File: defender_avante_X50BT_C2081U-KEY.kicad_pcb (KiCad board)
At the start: 2 copper layers, 172.7 x 61 mm, 85 parts, among them CN301 CONNECTOR_M_006_20_SPECIAL, J300 JUMPER, J301 JUMPER, J302 JUMPER, J303 JUMPER, J304 JUMPER, J305 JUMPER, J306 JUMPER, J307 JUMPER, J308 JUMPER, J309 JUMPER, J310 JUMPER, J311 JUMPER, J312 JUMPER, J313 JUMPER, J314 JUMPER, J315 JUMPER, J316 JUMPER, J317 JUMPER, J318 JUMPER, J319 JUMPER, J320 JUMPER, J321 JUMPER, J322 JUMPER, J323 JUMPER, J324 JUMPER, J325 JUMPER, J326 JUMPER, J327 JUMPER, J328 JUMPER, J329 JUMPER, J330 JUMPER, J331 JUMPER, J332 JUMPER, J333 JUMPER, J334 JUMPER, J335 JUMPER, J336 JUMPER, J337 JUMPER, Q300 BJT_NPN_GENERAL, U300 TM1668

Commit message: Исправлены связи новых резисторов. Удалены примитивы на слоях F.Cu и F.Mask
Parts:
- turned R306 to 90 degrees
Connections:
- D300 pad A: /E -> /KS1
- D301 pad A: /D -> /KS2
- D302 pad A: /DP -> /KS3
- D303 pad A: /C -> /KS4
- D304 pad A: /G -> /KS5
- R306 pad 1: V -> /IC_+5V
- R306 pad 2: /IC_+5V -> V
- R318 pad 1: Net-(R318-Pad1) -> /E
- R318 pad 2: /E -> /KS1
- R319 pad 1: Net-(R319-Pad1) -> /D
- R319 pad 2: /D -> /KS2
- R320 pad 1: Net-(R320-Pad1) -> /DP
- R320 pad 2: /DP -> /KS3
- R321 pad 1: Net-(R321-Pad1) -> /C
- R321 pad 2: /C -> /KS4
- R322 pad 1: Net-(R322-Pad1) -> /G
- R322 pad 2: /G -> /KS5
- R323 pad 1: Net-(R323-Pad1) -> /F
- R323 pad 2: /F -> Net-(R323-Pad2)
- R324 pad 2: /B -> /A
- R325 pad 2: /A -> /B
- U300 pad 1: Net-(U300-Pad1) -> /IC_DATA
- U300 pad 10: Net-(U300-Pad10) -> /KS4
- U300 pad 11: Net-(U300-Pad11) -> /KS5
- U300 pad 12: Net-(U300-Pad12) -> Net-(R323-Pad2)
- U300 pad 13: Net-(U300-Pad13) -> Net-(R325-Pad1)
- U300 pad 14: Net-(U300-Pad14) -> Net-(R324-Pad1)
- U300 pad 2: Net-(U300-Pad2) -> /IC_CLK
- U300 pad 20: Net-(U300-Pad20) -> /DIG4
- U300 pad 21: Net-(U300-Pad21) -> /DIG3
- U300 pad 22: Net-(U300-Pad22) -> COM
- U300 pad 23: Net-(U300-Pad23) -> /DIG2
- U300 pad 24: Net-(U300-Pad24) -> /DIG1
- U300 pad 3: Net-(U300-Pad3) -> /STB
- U300 pad 5: Net-(U300-Pad5) -> /K2
- U300 pad 6: Net-(U300-Pad6) -> /IC_+5V
- U300 pad 7: Net-(U300-Pad7) -> /KS1
- U300 pad 8: Net-(U300-Pad8) -> /KS2
- U300 pad 9: Net-(U300-Pad9) -> /KS3

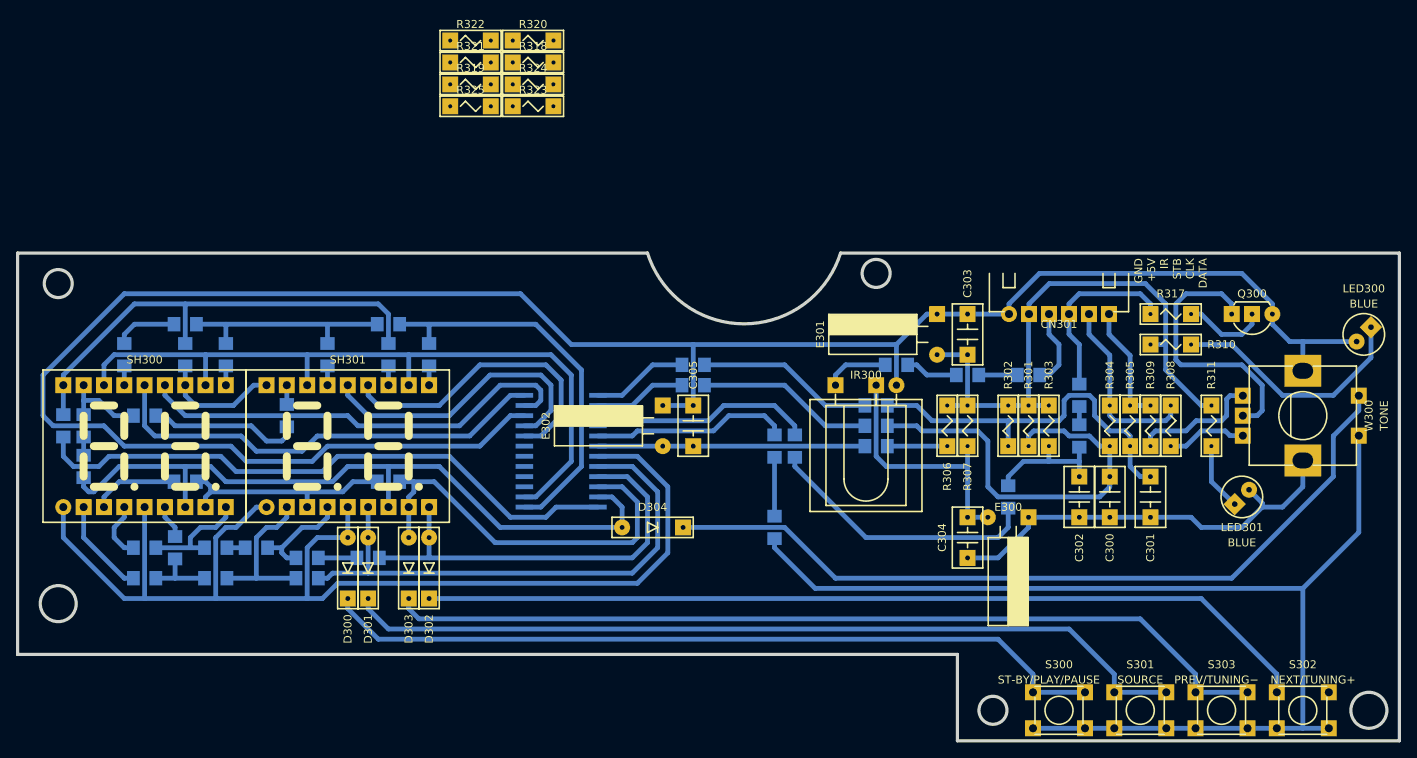
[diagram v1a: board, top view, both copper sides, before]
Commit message: Токоограничивающие резисторы размещены на плате. Плата отредактирована
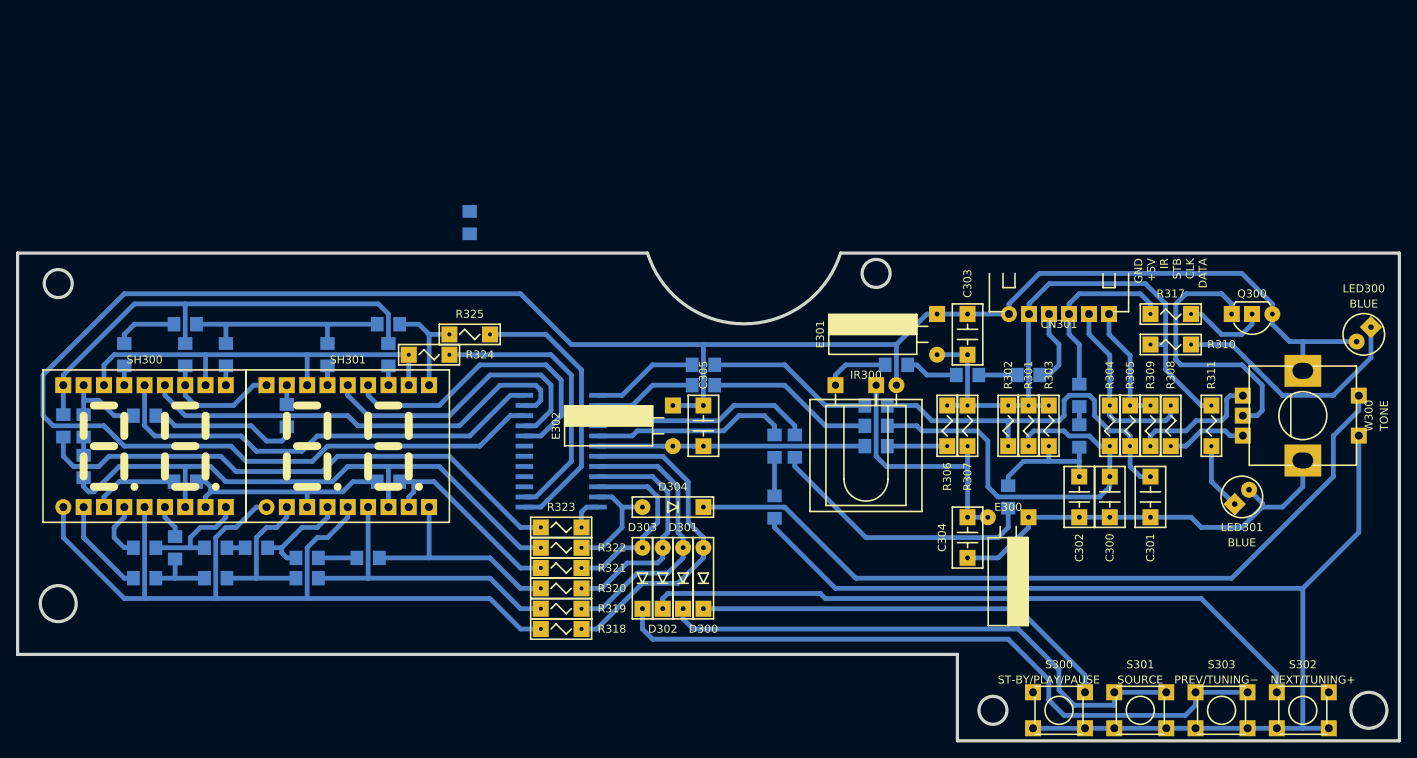
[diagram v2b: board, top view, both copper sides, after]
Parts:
- moved R318 70.9 mm to (129.5, 121.9)
- moved R320 68.6 mm to (129.5, 116.8)
- moved R319 66.5 mm to (129.5, 119.4)
- moved R322 64.4 mm to (129.5, 111.8)
- moved R321 64.2 mm to (129.5, 114.3)
- moved R323 52.8 mm to (129.5, 109.2)
- moved D300 44.5 mm to (147.3, 115.6)
- moved D301 39.4 mm to (144.8, 115.6)
- moved R324 36.2 mm to (113.0, 87.6), turned to 180 degrees
- moved D302 29.2 mm to (142.2, 115.6)
- moved D303 29.2 mm to (139.7, 115.6)
- moved R325 28.5 mm to (118.1, 85.1), turned to 180 degrees
- moved J314 17.3 mm to (118.1, 71.1)
- moved D304 3.59 mm to (143.5, 106.7)
- moved J311 2.54 mm to (156.2, 106.7)
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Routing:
- net Net-(D300-PadC): track 99.1 -> 53.3 mm
- net /KS1: track 0.00 -> 41.8 mm
- net /A: track 92.5 -> 52.6 mm
- net /B: track 93.8 -> 55.6 mm
- net Net-(D301-PadC): track 106.7 -> 69.2 mm
- net /E: track 146.2 -> 109.5 mm
- net /KS2: track 0.00 -> 35.5 mm
- net Net-(R324-Pad1): track 0.00 -> 34.8 mm
- net Net-(R325-Pad1): track 0.00 -> 34.6 mm
- net /KS3: track 0.00 -> 29.8 mm
- net /D: track 112.7 -> 83.0 mm
- net Net-(D302-PadC): track 112.2 -> 84.7 mm
- net /DP: track 95.1 -> 69.6 mm
- net Net-(D303-PadC): track 111.8 -> 86.3 mm
- net /C: track 89.5 -> 64.5 mm
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
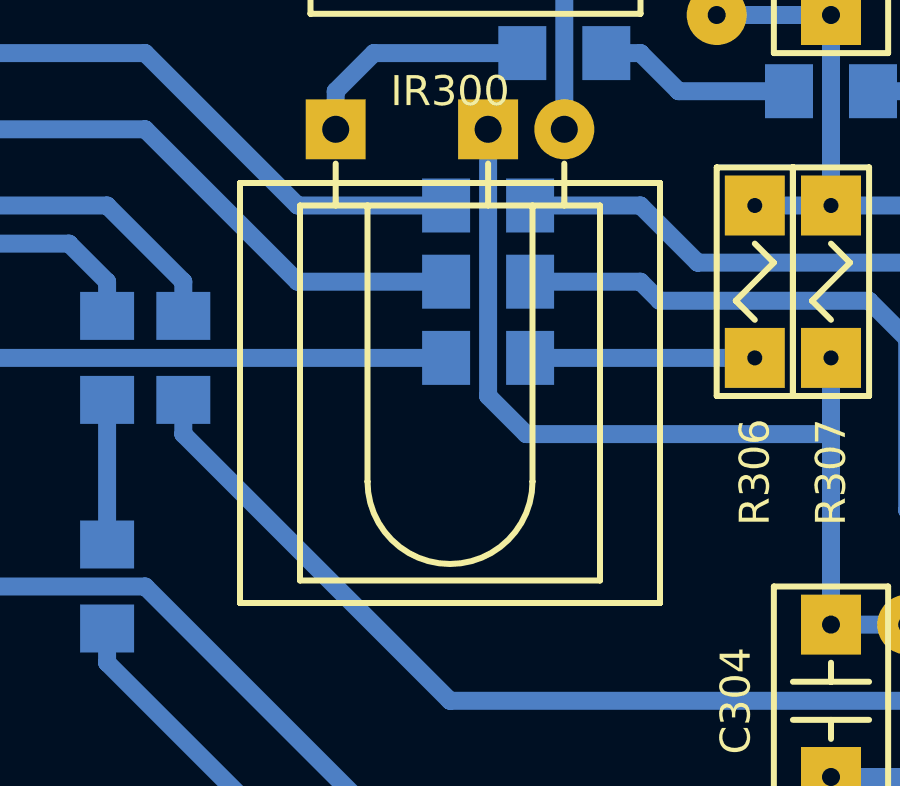
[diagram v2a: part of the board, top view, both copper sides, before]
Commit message: Удалён поролоновый держатель
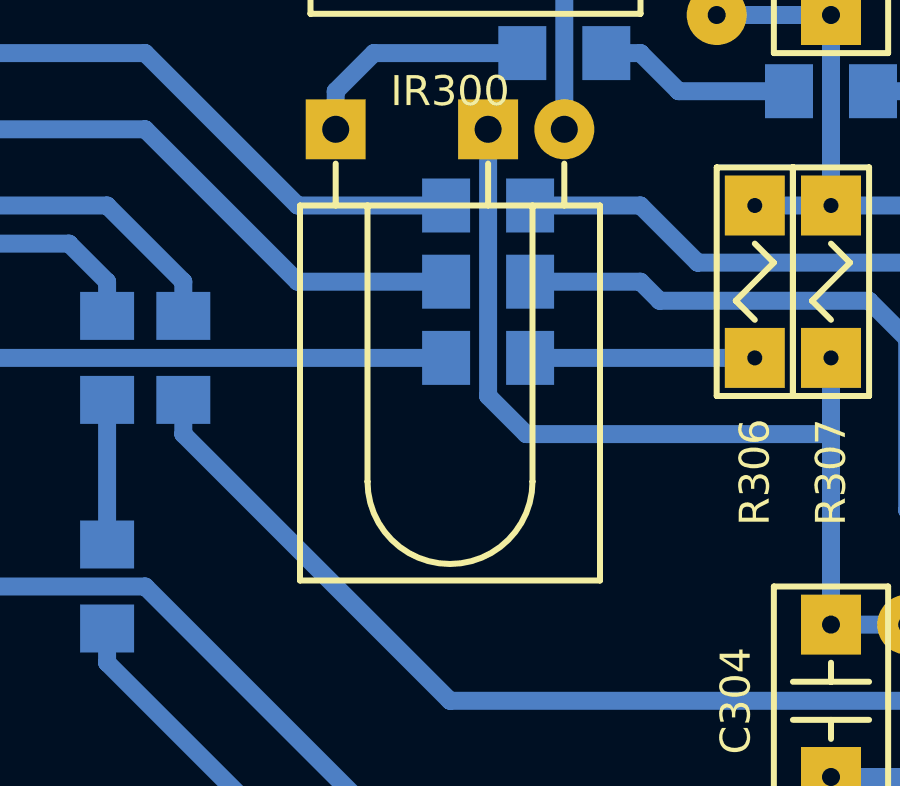
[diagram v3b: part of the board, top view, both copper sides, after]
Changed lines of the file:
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@@
   (general
     (thickness 1.5)
-    (drawings 39)
+    (drawings 27)
     (tracks 502)
     (zones 0)
@@
   (title_block
     (title defender_avante_X50BT_C2081U-KEY)
-    (date 2019-05-16)
+    (date 2019-05-23)
     (rev 2)
     (company "Igor Vladimirovich Ivanov")
@@
       (effects (font (size 1 1) (thickness 0.2)))
     )
-    (fp_text value DIODE_GENERAL (at 15.875 0 270) (layer F.Fab) hide
+    (fp_text value DIODE_GENERAL (at 1.905 -7.62) (layer F.Fab) hide
       (effects (font (size 1 1) (thickness 0.2)))
     )
@@
       (effects (font (size 1 1) (thickness 0.2)))
     )
-    (fp_text value DIODE_GENERAL (at 15.875 0 270) (layer F.Fab) hide
+    (fp_text value DIODE_GENERAL (at -1.905 -15.24) (layer F.Fab) hide
       (effects (font (size 1 1) (thickness 0.2)))
     )
@@
       (effects (font (size 1 1) (thickness 0.2)))
     )
-    (fp_text value DIODE_GENERAL (at 15.875 0 270) (layer F.Fab) hide
+    (fp_text value DIODE_GENERAL (at -0.635 -12.7) (layer F.Fab) hide
       (effects (font (size 1 1) (thickness 0.2)))
     )
@@
       (effects (font (size 1 1) (thickness 0.2)))
     )
-    (fp_text value RESISTOR_GENERAL (at -17.145 -22.86 180) (layer F.Fab) hide
+    (fp_text value RESISTOR_GENERAL (at -15.875 -22.86 180) (layer F.Fab) hide
       (effects (font (size 1 1) (thickness 0.2)))
     )
@@
       (effects (font (size 1 1) (thickness 0.2)))
     )
-    (fp_text value RESISTOR_GENERAL (at -13.335 -12.7 180) (layer F.Fab) hide
+    (fp_text value RESISTOR_GENERAL (at -12.065 -12.7 180) (layer F.Fab) hide
       (effects (font (size 1 1) (thickness 0.2)))
     )
@@
       (effects (font (size 1 1) (thickness 0.2)))
     )
-    (fp_text value RESISTOR_GENERAL (at -15.875 -20.32 180) (layer F.Fab) hide
+    (fp_text value RESISTOR_GENERAL (at -14.605 -20.32 180) (layer F.Fab) hide
       (effects (font (size 1 1) (thickness 0.2)))
     )
@@
       (effects (font (size 1 1) (thickness 0.2)))
     )
-    (fp_text value RESISTOR_GENERAL (at -12.065 -10.16) (layer F.Fab) hide
+    (fp_text value RESISTOR_GENERAL (at -10.795 -10.16) (layer F.Fab) hide
       (effects (font (size 1 1) (thickness 0.2)))
     )
@@
       (effects (font (size 1 1) (thickness 0.2)))
     )
-    (fp_text value RESISTOR_GENERAL (at -14.605 -17.78 180) (layer F.Fab) hide
+    (fp_text value RESISTOR_GENERAL (at -13.335 -17.78 180) (layer F.Fab) hide
       (effects (font (size 1 1) (thickness 0.2)))
     )
@@
       (effects (font (size 1 1) (thickness 0.2)))
     )
-    (fp_text value DIODE_GENERAL (at 15.875 0 270) (layer F.Fab) hide
+    (fp_text value DIODE_GENERAL (at 0.635 -10.16) (layer F.Fab) hide
       (effects (font (size 1 1) (thickness 0.2)))
     )
@@
       (net 4 "Net-(R308-Pad1)"))
   )
-  (gr_line (start 160.64 93.23) (end 174.64 93.23) (layer F.SilkS) (width 0.2))
-  (gr_line (start 160.64 107.23) (end 174.64 107.23) (layer F.SilkS) (width 0.2))
-  (gr_line (start 160.64 93.23) (end 174.64 93.23) (layer F.CrtYd) (width 0.1))
-  (gr_line (start 160.64 93.23) (end 174.64 93.23) (layer F.Fab) (width 0.2))
-  (gr_line (start 160.64 107.23) (end 174.64 107.23) (layer F.CrtYd) (width 0.1))
-  (gr_line (start 174.64 93.23) (end 174.64 107.23) (layer F.CrtYd) (width 0.1))
-  (gr_line (start 160.64 93.23) (end 160.64 107.23) (layer F.CrtYd) (width 0.1))
-  (gr_line (start 174.64 93.23) (end 174.64 107.23) (layer F.SilkS) (width 0.2))
-  (gr_line (start 160.64 93.23) (end 160.64 107.23) (layer F.SilkS) (width 0.2))
   (gr_text "GND\n+5V\nIR\nSTB\nCLK\nDATA" (at 205.74 75.565 90) (layer F.SilkS)
     (effects (font (size 1 1) (thickness 0.2)) (justify right))
   )
-  (gr_line (start 160.64 93.23) (end 160.64 107.23) (layer F.Fab) (width 0.2))
   (gr_text TONE (at 232.41 95.25 90) (layer F.SilkS)
     (effects (font (size 1 1) (thickness 0.2)))
   )
-  (gr_line (start 174.64 93.23) (end 174.64 107.23) (layer F.Fab) (width 0.2))
   (gr_text BLUE (at 214.63 111.125) (layer F.SilkS)
     (effects (font (size 1 1) (thickness 0.2)))
@@
     (effects (font (size 1 1) (thickness 0.2)))
   )
-  (gr_line (start 160.64 107.23) (end 174.64 107.23) (layer F.Fab) (width 0.2))
   (gr_circle (center 229.87 85.09) (end 232.47 85.09) (layer F.SilkS) (width 0.2))
   (gr_circle (center 229.87 85.09) (end 232.47 85.09) (layer F.Fab) (width 0.2))
@@
   (segment (start 113.03 85.09) (end 115.57 85.09) (width 0.6) (layer B.Cu) (net 16))
   (segment (start 111.76 83.82) (end 113.03 85.09) (width 0.6) (layer B.Cu) (net 16))
-  (segment (start 126.365 105.41) (end 130.81 100.965) (width 0.6) (layer B.Cu) (net 42))
-  (segment (start 126.365 105.41) (end 124.94 105.41) (width 0.6) (layer B.Cu) (net 42))
-  (segment (start 130.81 90.17) (end 130.81 100.965) (width 0.6) (layer B.Cu) (net 42))
   (segment (start 110.49 87.63) (end 110.49 91.44) (width 0.6) (layer B.Cu) (net 17))
   (segment (start 97.79 87.63) (end 97.79 91.44) (width 0.6) (layer B.Cu) (net 17))
@@
   (segment (start 72.39 91.44) (end 72.39 88.9) (width 0.6) (layer B.Cu) (net 17))
   (segment (start 72.39 88.9) (end 73.66 87.63) (width 0.6) (layer B.Cu) (net 17))
-  (segment (start 128.27 87.63) (end 130.81 90.17) (width 0.6) (layer B.Cu) (net 42))
   (segment (start 91.11 91.44) (end 88.57 93.98) (width 0.6) (layer B.Cu) (net 18))
   (segment (start 92.71 91.44) (end 91.11 91.44) (width 0.6) (layer B.Cu) (net 18))
@@
   (segment (start 127 106.68) (end 132.08 101.6) (width 0.6) (layer B.Cu) (net 41))
   (segment (start 120.65 85.09) (end 127.635 85.09) (width 0.6) (layer B.Cu) (net 41))
+  (segment (start 126.365 105.41) (end 130.81 100.965) (width 0.6) (layer B.Cu) (net 42))
+  (segment (start 126.365 105.41) (end 124.94 105.41) (width 0.6) (layer B.Cu) (net 42))
+  (segment (start 130.81 90.17) (end 130.81 100.965) (width 0.6) (layer B.Cu) (net 42))
+  (segment (start 128.27 87.63) (end 130.81 90.17) (width 0.6) (layer B.Cu) (net 42))
   (segment (start 128.27 87.63) (end 115.57 87.63) (width 0.6) (layer B.Cu) (net 42))
   (segment (start 132.08 111.76) (end 134.62 111.76) (width 0.6) (layer B.Cu) (net 43))
